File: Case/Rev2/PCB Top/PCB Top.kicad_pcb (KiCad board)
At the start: 2 copper layers, 146.6 x 89 mm, 27 parts

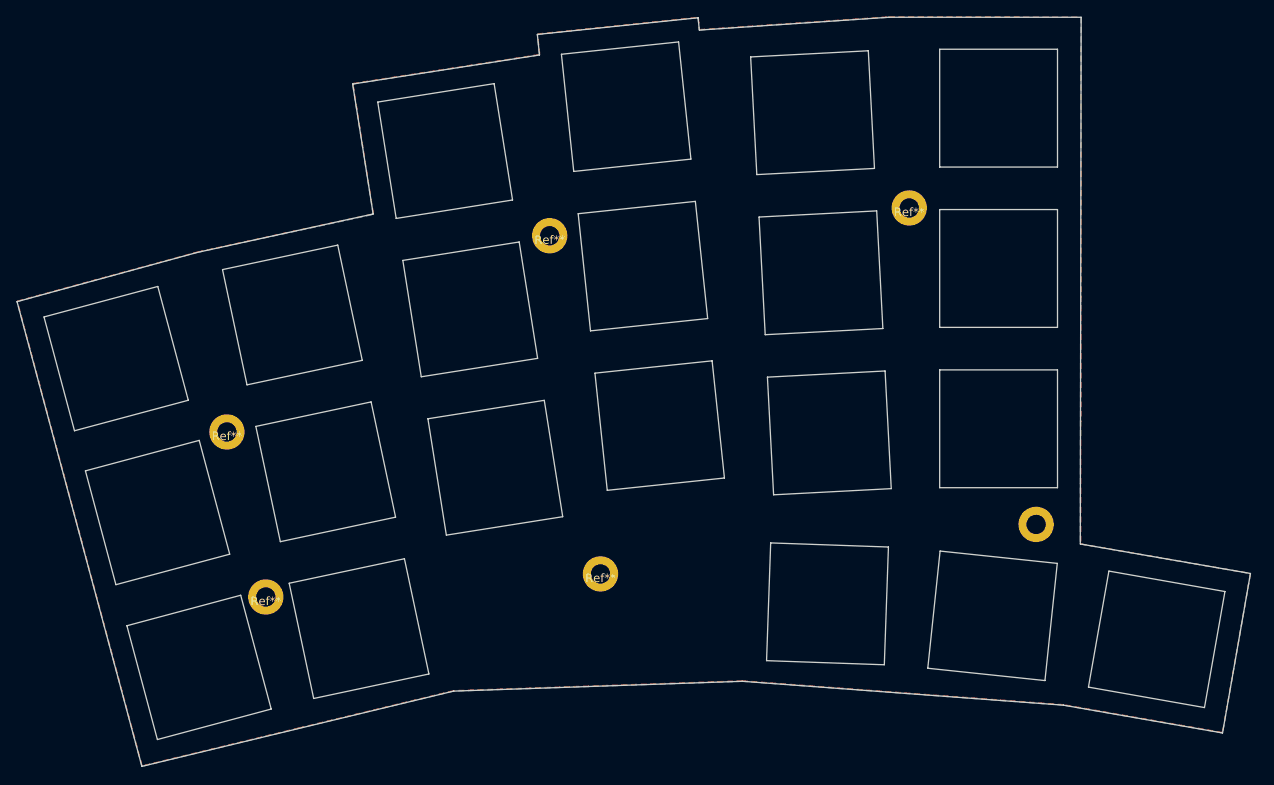
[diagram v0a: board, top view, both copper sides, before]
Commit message: update thumb cluster since its too close to amphenol cutout
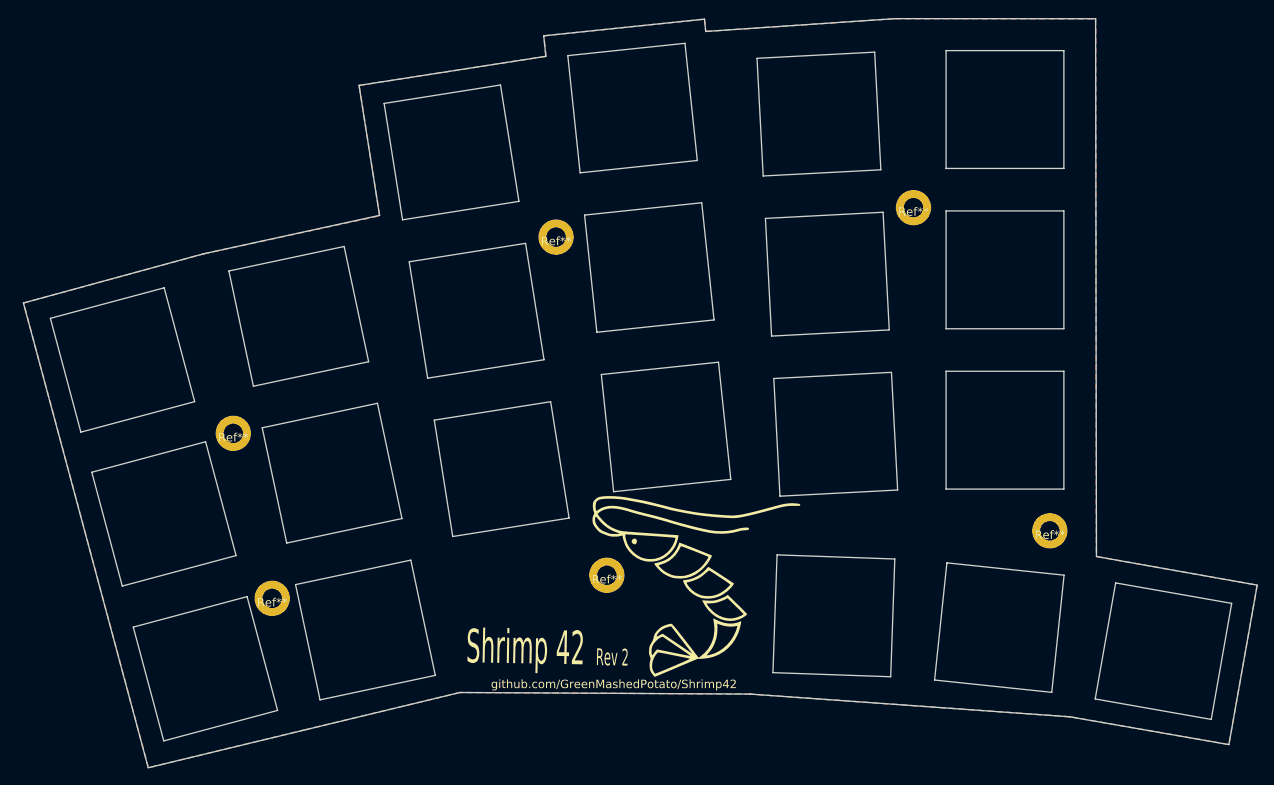
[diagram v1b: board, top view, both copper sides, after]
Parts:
- removed ?: , 
- removed the Ref** at (120.4, 40.2)
- removed the Ref** at (83.7, 83.7)
- removed the Ref** at (77.6, 43.5)
- removed the Ref** at (43.9, 86.4)
- removed the Ref** at (39.3, 66.8)
- added G***: LOGO, footprints:Shrimp_small_small, F.Cu at (94.1, 86.8)
- added Ref**: Val**, footprints:hole-m2, F.Cu at (137.1, 78.5)
- added Ref**: Val**, footprints:hole-m2, F.Cu at (40.0, 67.0)
- added Ref**: Val**, footprints:hole-m2, F.Cu at (44.7, 86.6)
- added Ref**: Val**, footprints:hole-m2, F.Cu at (78.4, 43.6)
- added Ref**: Val**, footprints:hole-m2, F.Cu at (84.4, 83.8)
- added Ref**: Val**, footprints:hole-m2, F.Cu at (120.9, 40.1)
- moved K-3-5 1.62 mm to (150.6, 92.8)
- moved K-3-4 1.62 mm to (131.1, 90.0)
- moved K-3-3 1.61 mm to (111.4, 88.6)
- moved K-1-2 0.78 mm to (68.9, 52.4)
- moved K-1-0 0.78 mm to (31.8, 76.5)
- moved K-2-1 0.78 mm to (55.7, 90.3)
- moved K-0-2 0.78 mm to (66.0, 33.6)
- moved K-1-3 0.78 mm to (89.5, 47.3)
- moved K-1-4 0.78 mm to (110.6, 48.1)
- moved K-0-3 0.78 mm to (87.5, 28.3)
- moved K-0-4 0.78 mm to (109.6, 29.0)
- moved K-0-0 0.78 mm to (26.9, 58.2)
- moved K-0-1 0.78 mm to (47.8, 53.1)
- moved K-1-1 0.78 mm to (51.8, 71.7)
- moved K-2-0 0.78 mm to (36.7, 94.9)
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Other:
- outline, holes or cut-outs redrawn
- board text added: "Rev 2"
- board text added: "Shrimp 42"
- board text added: "github.com/GreenMashedPotato/Shrimp42"
